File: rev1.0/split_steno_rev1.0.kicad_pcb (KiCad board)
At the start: 2 copper layers, 97.6 x 84.5 mm, 50 parts, among them J0 Audio-Jack-4, K0 KEYSW, K1 KEYSW, K10 KEYSW, K11 KEYSW, K12 KEYSW, K13 KEYSW, K14 KEYSW, K15 KEYSW, K16 KEYSW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

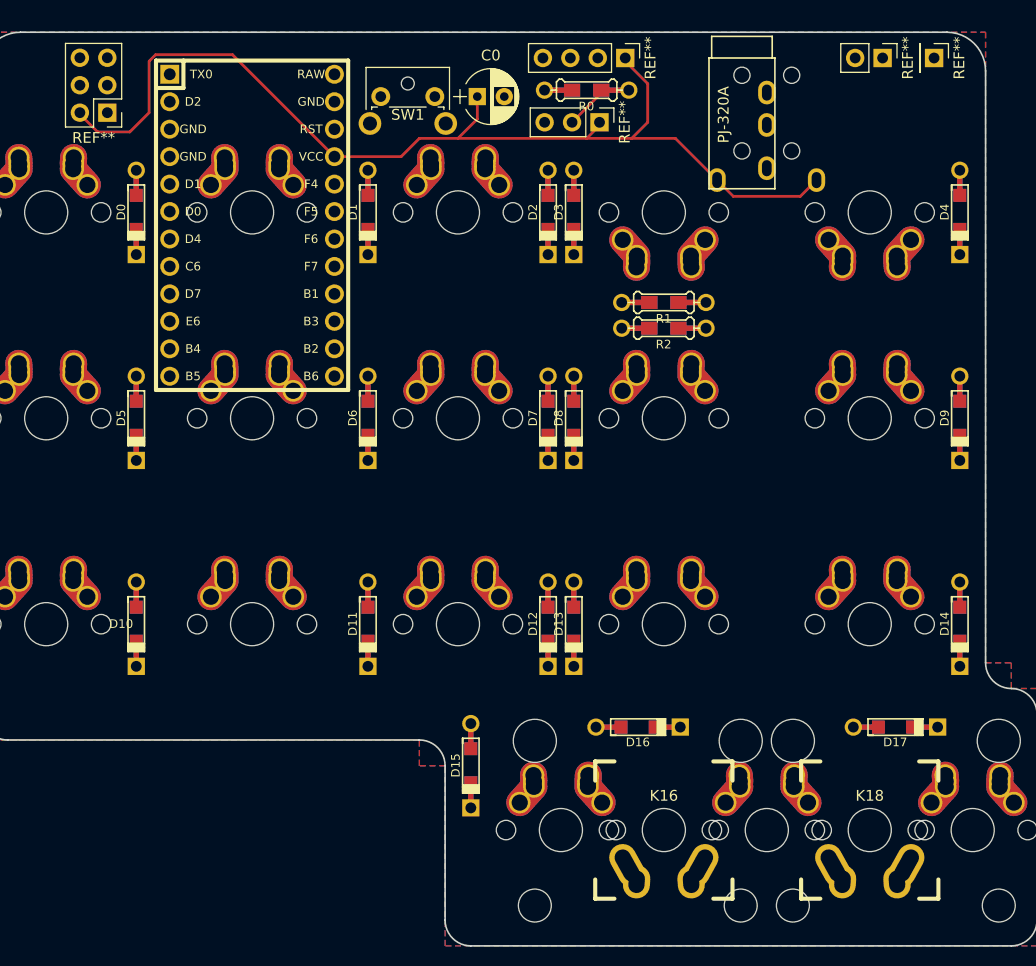
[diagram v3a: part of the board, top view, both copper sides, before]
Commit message: updated schematic and footprints
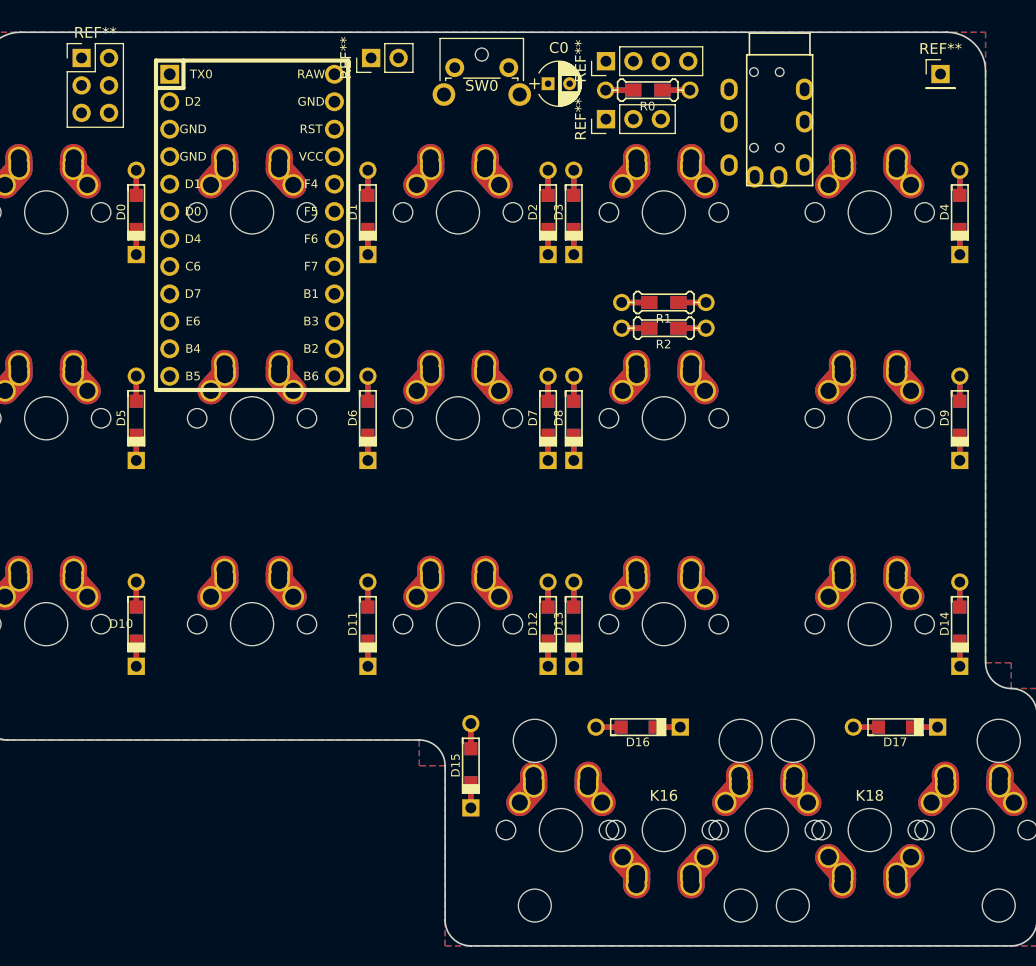
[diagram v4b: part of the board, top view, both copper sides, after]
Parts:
- removed SW1: SW_PUSH, Keebio-Parts:SW_Tactile_SPST_Angled_MJTP1117
- added G***: LOGO, airi_logo:airi_icon-7.6, F.Cu at (126.2, 96.1)
- added G***: LOGO, airi_logo:airi_icon-7.6, B.Cu at (126.2, 96.1)
- added REF**: TRRS-PJ-320A, Keebio-Parts:TRRS-PJ-320A, B.Cu at (172.6, 73.5)
- added SW0: SW_PUSH, Keebio-Parts:SW_Tactile_SPST_Angled_MJTP1117, F.Cu at (145.0, 74.7)
- C0: footprint Capacitors_THT:CP_Radial_D5.0mm_P2.50mm -> Capacitors_THT:CP_Radial_D4.0mm_P2.00mm
- J0: footprint Keebio-Parts:TRRS-PJ-320A-dual -> Keebio-Parts:TRRS-PJ-320A
- K16, K18: footprint Keebio-Parts:Hybrid_PCB_200H-dual -> Keebio-Parts:Hybrid_PCB_200H-dual-nosilk
- REF**: value EXTRA -> PWM
- moved REF** 47.3 mm to (137.2, 73.8), turned to 90 degrees
- moved C0 6.66 mm to (153.6, 76.2)
- moved R0 5.66 mm to (162.8, 76.8)
- moved REF** 5.59 mm to (110.4, 73.8), turned to 0 degrees
- moved REF** 1.81 mm to (158.9, 74.1), turned to 90 degrees
- moved REF** 1.60 mm to (189.9, 75.3), turned to 0 degrees
- moved J0 1.23 mm to (175.0, 73.5)
- moved REF** 0.67 mm to (158.9, 79.5), turned to 90 degrees
- turned K3 to 0 degrees
- turned K4 to 0 degrees
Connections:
- net /col1 renamed /c1
- net Net-(U0-Pad1) renamed /tx
- net Net-(U0-Pad14) renamed /miso
- net Net-(U0-Pad15) renamed /sclk
- net Net-(U0-Pad16) renamed /mosi
- D0 pad 1: /row0 -> /r0
- D1 pad 1: /row0 -> /r0
- D10 pad 1: /row2 -> /r2
- D11 pad 1: /row2 -> /r2
- D12 pad 1: /row2 -> /r2
- D13 pad 1: /row2 -> /r2
- D14 pad 1: /row2 -> /r2
- D15 pad 1: /row3 -> /r3
- D16 pad 1: /row3 -> /r3
- D17 pad 1: /row3 -> /r3
- D2 pad 1: /row0 -> /r0
- D3 pad 1: /row0 -> /r0
- D4 pad 1: /row0 -> /r0
- D5 pad 1: /row1 -> /r1
- D6 pad 1: /row1 -> /r1
- D7 pad 1: /row1 -> /r1
- D8 pad 1: /row1 -> /r1
- D9 pad 1: /row1 -> /r1
- J0 pad 1: VCC -> /d0
- J0 pad 2: /data0 -> /d1
- J0 pad 3: /data1 -> VCC
- K0 pad 1: /col0 -> /c0
- K10 pad 1: /col0 -> /c0
- K12 pad 1: /col2 -> /c2
- K13 pad 1: /col3 -> /c3
- K14 pad 1: /col4 -> /c4
- K15 pad 1: /col2 -> /c2
- K16 pad 1: /col3 -> /c3
- K17 pad 1: /col3 -> /c3
- K18 pad 1: /col4 -> /c4
- K19 pad 1: /col4 -> /c4
- K2 pad 1: /col2 -> /c2
- K3 pad 1: /col3 -> /c3
- K4 pad 1: /col4 -> /c4
- K5 pad 1: /col0 -> /c0
- K7 pad 1: /col2 -> /c2
- K8 pad 1: /col3 -> /c3
- K9 pad 1: /col4 -> /c4
- R0 pad 2: /rgb0 -> /d2
- R1 pad 1: /data0 -> VCC
- R1 pad 2: VCC -> /d1
- R2 pad 1: /data1 -> VCC
- R2 pad 2: VCC -> /d0
- REF** pad 2: VCC -> (no net)
- REF** pad 6: GND -> (no net)
- REF** pad 1: VCC -> (no net) (x2)
- REF** pad 2: GND -> (no net) (x2)
- REF** pad 2: /dout -> (no net)
- REF** pad 3: GND -> (no net)
- U0 pad 10: /rgb0 -> /pwm
- U0 pad 18: /row3 -> /r0
- U0 pad 19: /row2 -> /c4
- U0 pad 2: /data0 -> /d0
- U0 pad 20: /row1 -> /c3
- U0 pad 21: VCC -> /c2
- U0 pad 23: GND -> (no net)
- U0 pad 3: GND -> /d1
- U0 pad 4: GND -> /d2
- U0 pad 5: Net-(U0-Pad5) -> /c0
- U0 pad 7: /col2 -> /r1
- U0 pad 8: /col3 -> /r2
- U0 pad 9: /col4 -> /r3
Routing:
- net VCC: track 97.7 -> 0.00 mm
- net /dout: track 6.48 -> 0.00 mm

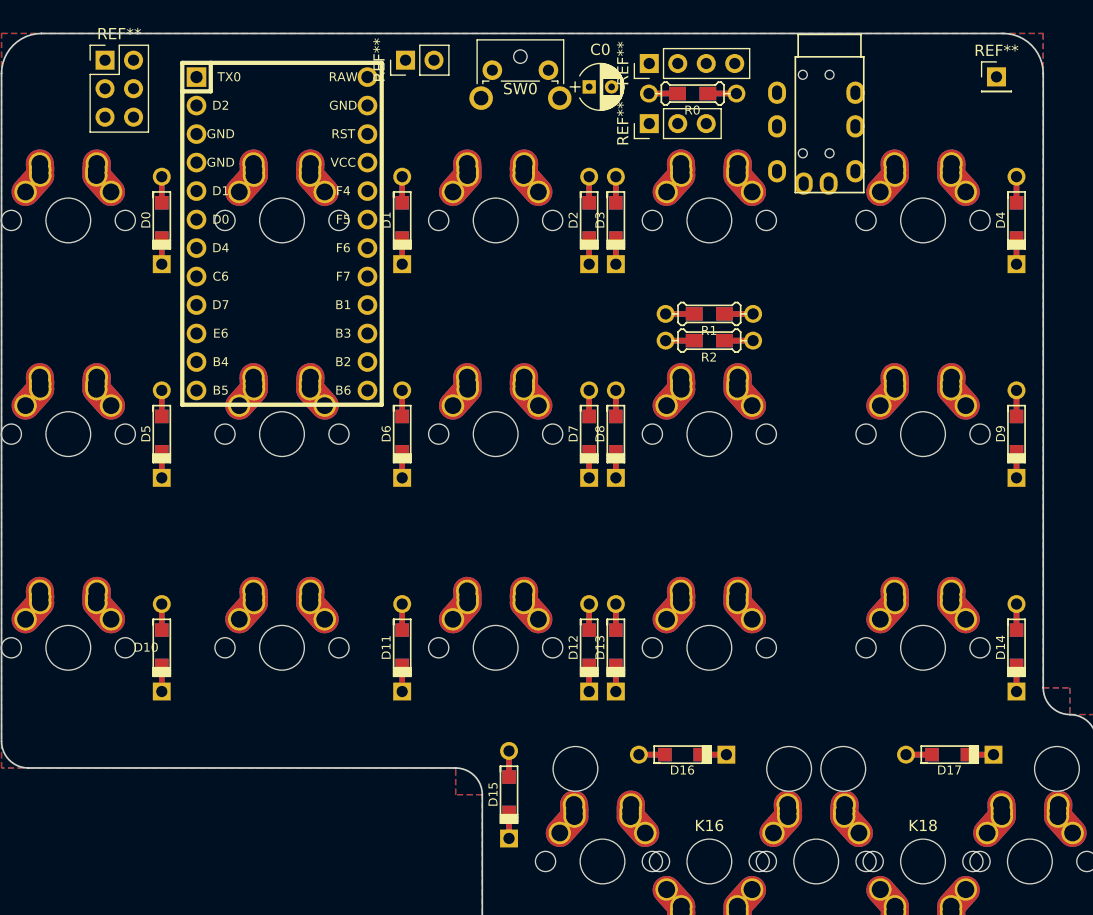
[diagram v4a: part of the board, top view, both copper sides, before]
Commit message: rearranged footprints
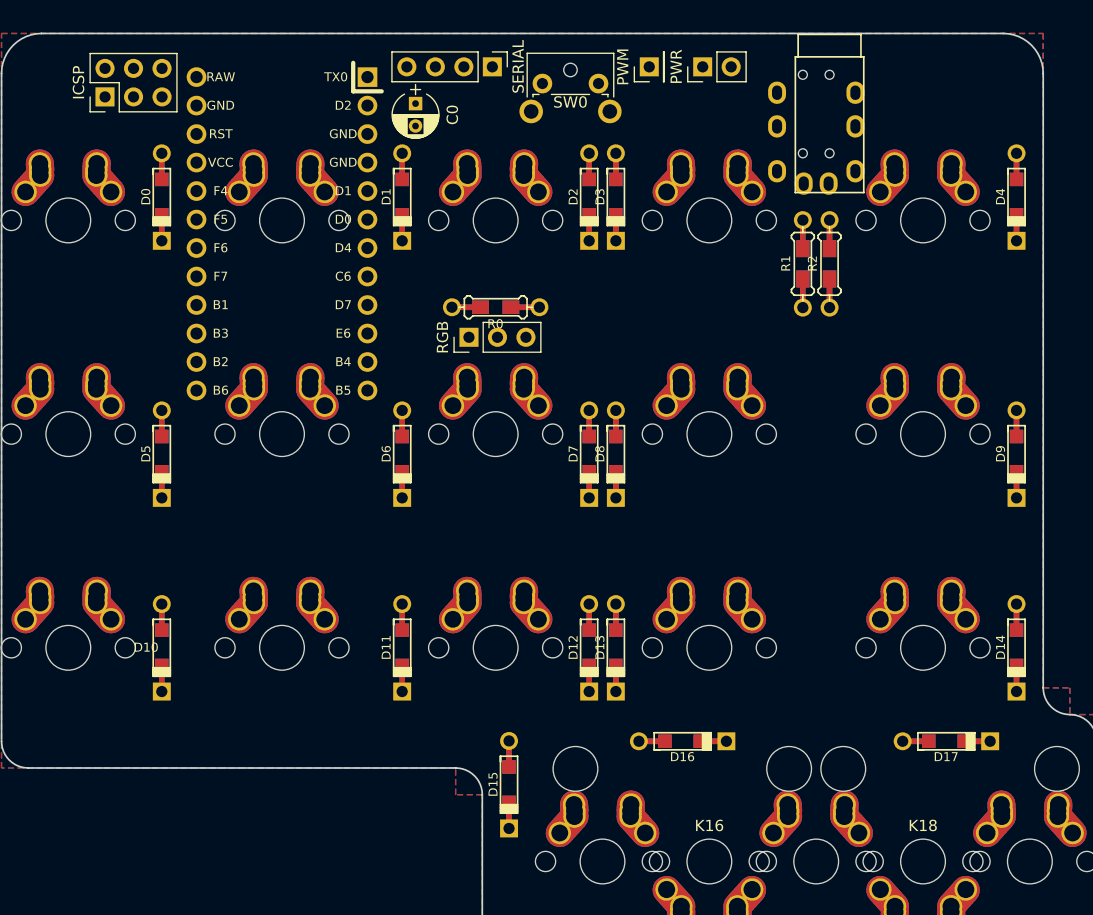
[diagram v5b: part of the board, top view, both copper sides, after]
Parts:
- removed G*** (x2): LOGO, airi_logo:airi_icon-7.6
- J0: value Audio-Jack-4 -> TRRS
- REF**: value TRRS-PJ-320A -> TRRS
- U0: moved to B.Cu
- moved PWM 31.0 mm to (158.9, 74.4), turned to 90 degrees
- moved PWR 26.5 mm to (163.7, 74.4)
- moved R0 25.9 mm to (145.3, 95.8)
- moved RGB 24.9 mm to (142.9, 98.5)
- moved C0 15.5 mm to (138.1, 77.7), turned to 270 degrees
- moved SERIAL 14.0 mm to (145.0, 74.4), turned to 270 degrees
- moved R2 12.7 mm to (175.0, 92.0), turned to 270 degrees
- moved R1 9.46 mm to (172.6, 92.0), turned to 270 degrees
- moved SW0 4.62 mm to (149.4, 75.9)
- moved ICSP 3.27 mm to (110.4, 77.1), turned to 90 degrees
- moved D4 2.08 mm to (191.7, 86.0)
- moved D3 2.08 mm to (156.0, 86.0)
- moved D2 2.08 mm to (153.6, 86.0)
- moved D1 2.08 mm to (136.9, 86.0)
- moved D0 2.08 mm to (115.5, 86.0)
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- renumbered REF** to ICSP, REF** to PWM, REF** to PWR, REF** to RGB, REF** to SERIAL
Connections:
- ICSP pad 1: (no net) -> /miso
- ICSP pad 2: (no net) -> VCC
- ICSP pad 3: (no net) -> /sclk
- ICSP pad 4: (no net) -> /mosi
- ICSP pad 6: (no net) -> GND
- PWR pad 2: (no net) -> GND
- REF** pad 1: (no net) -> /d0
- REF** pad 2: (no net) -> /d1
- RGB pad 1: (no net) -> VCC
- RGB pad 2: (no net) -> /dout
- RGB pad 3: (no net) -> GND
- SERIAL pad 1: (no net) -> VCC
- SERIAL pad 2: (no net) -> GND

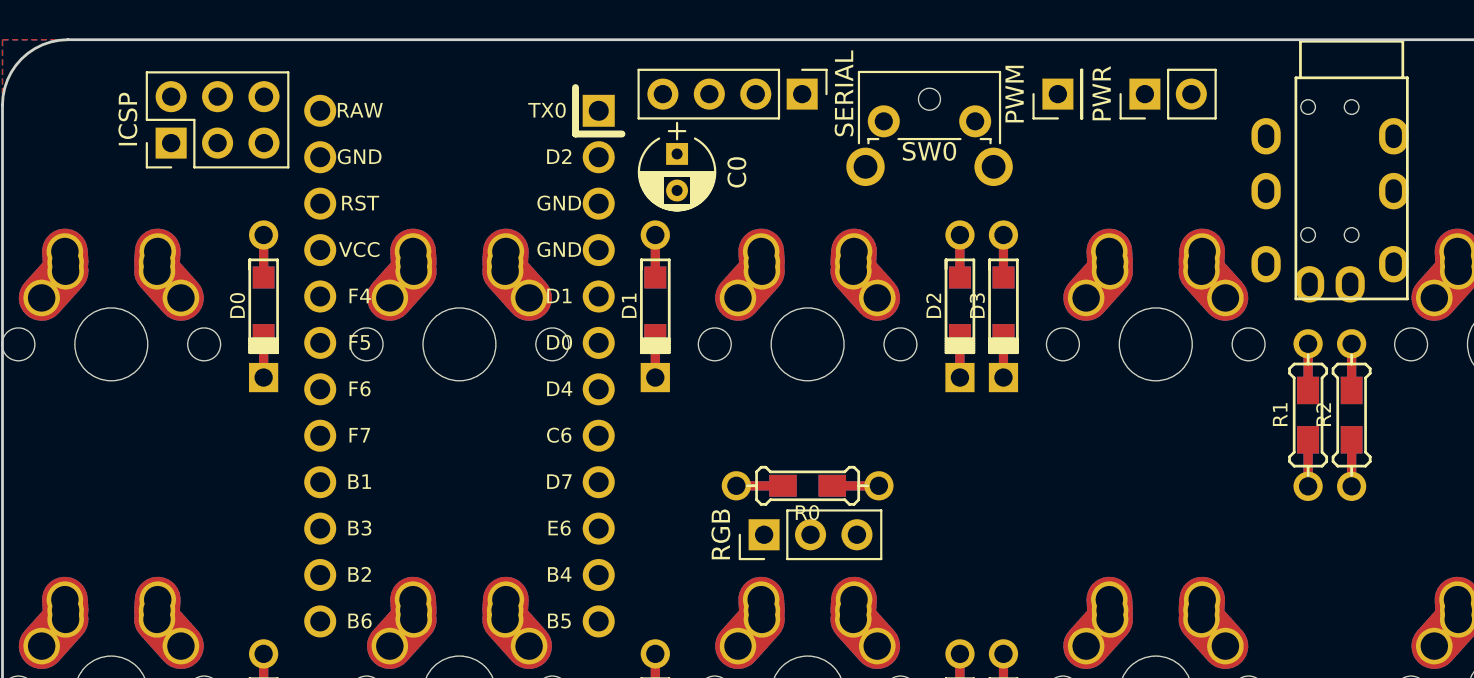
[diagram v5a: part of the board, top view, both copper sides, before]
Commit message: reorganized schematic library and pro micro footprint
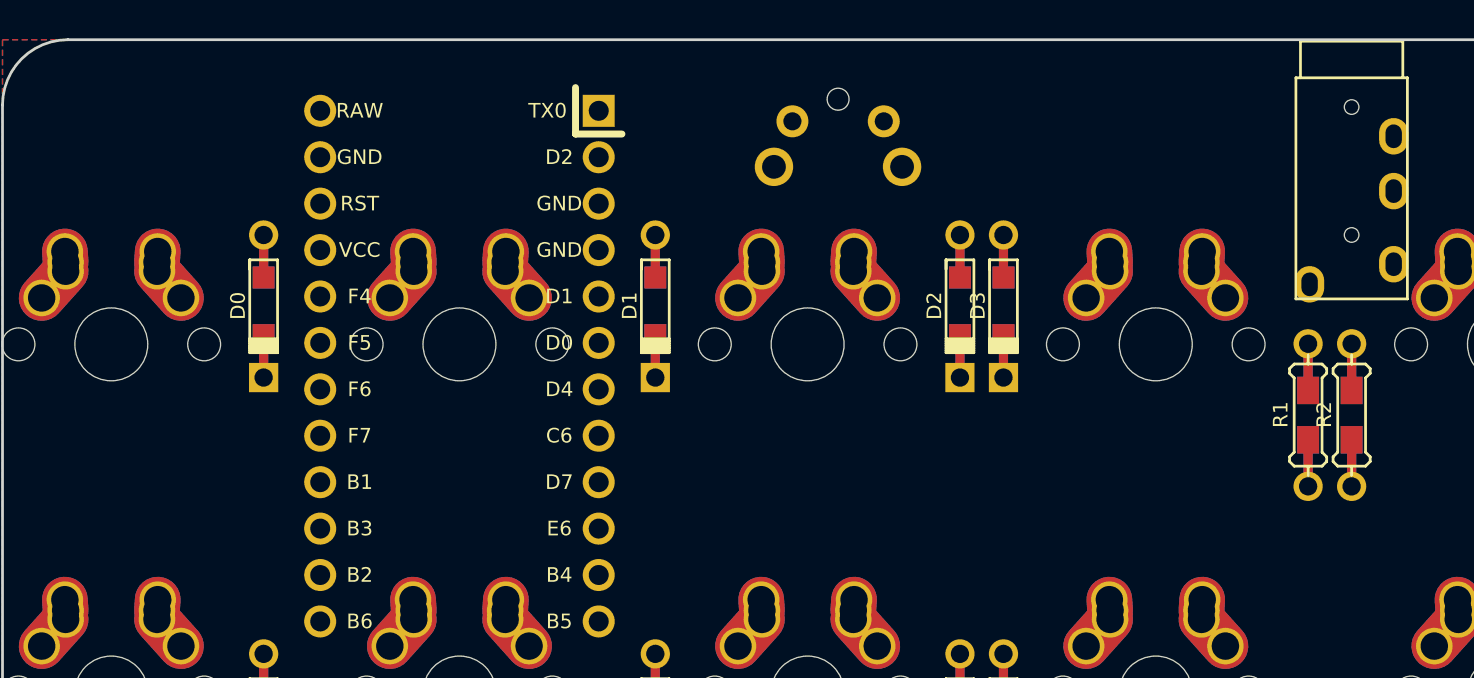
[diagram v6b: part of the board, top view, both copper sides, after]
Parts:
- removed C0: CP, Capacitors_THT:CP_Radial_D4.0mm_P2.00mm
- removed ICSP: ICSP, Pin_Headers:Pin_Header_Straight_2x03_Pitch2.54mm
- removed PWM: PWM, Pin_Headers:Pin_Header_Straight_1x01_Pitch2.54mm
- removed PWR: PWR, Pin_Headers:Pin_Header_Straight_1x02_Pitch2.54mm
- removed R0: 500, Keebio-Parts:Resistor-Hybrid
- removed REF**: TRRS, Keebio-Parts:TRRS-PJ-320A
- removed RGB: RGB, Pin_Headers:Pin_Header_Straight_1x03_Pitch2.54mm
- removed SERIAL: SERIAL, Pin_Headers:Pin_Header_Straight_1x04_Pitch2.54mm
- J0: value TRRS -> Audio-Jack-4
- SW0: moved to B.Cu
- turned SW0 to 180 degrees
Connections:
- U0 pad 10: /pwm -> /r1
- U0 pad 11: (no net) -> /r2
- U0 pad 12: (no net) -> /r3
- U0 pad 13: (no net) -> Net-(U0-Pad13)
- U0 pad 14: /miso -> Net-(U0-Pad14)
- U0 pad 15: /sclk -> Net-(U0-Pad15)
- U0 pad 16: /mosi -> Net-(U0-Pad16)
- U0 pad 17: (no net) -> /r0
- U0 pad 18: /r0 -> /c4
- U0 pad 19: /c4 -> /c3
- U0 pad 2: /d0 -> Net-(U0-Pad2)
- U0 pad 20: /c3 -> /c2
- U0 pad 21: /c2 -> VCC
- U0 pad 22: (no net) -> Net-(SW0-Pad1)
- U0 pad 23: (no net) -> GND
- U0 pad 24: (no net) -> Net-(U0-Pad24)
- U0 pad 3: /d1 -> GND
- U0 pad 4: /d2 -> GND
- U0 pad 5: /c0 -> /d0
- U0 pad 6: /c1 -> /d1
- U0 pad 7: /r1 -> Net-(U0-Pad7)
- U0 pad 8: /r2 -> /c0
- U0 pad 9: /r3 -> /c1

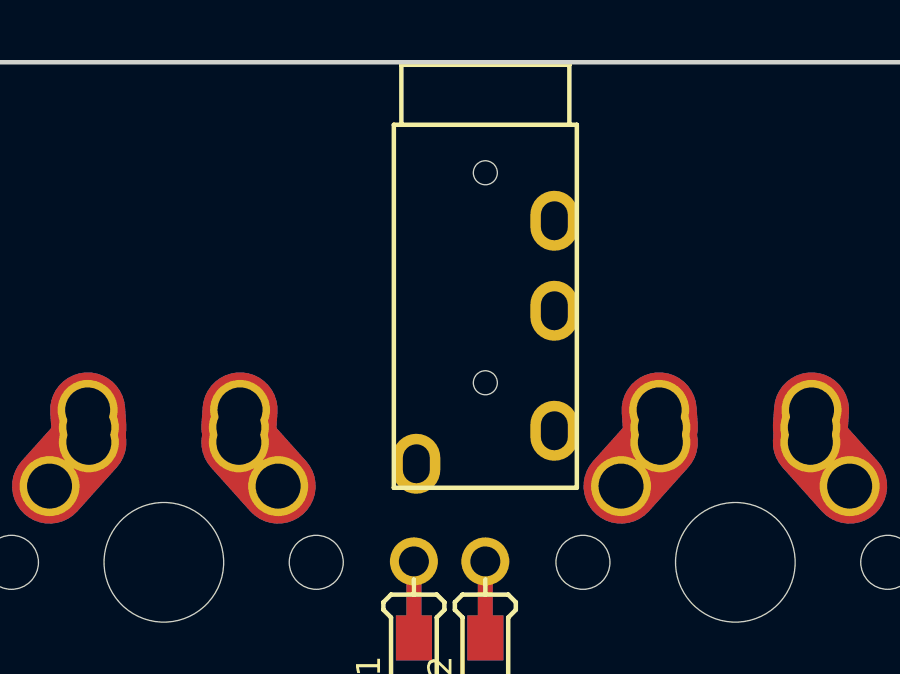
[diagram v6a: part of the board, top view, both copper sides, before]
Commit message: removed global libraries and moved to local versions
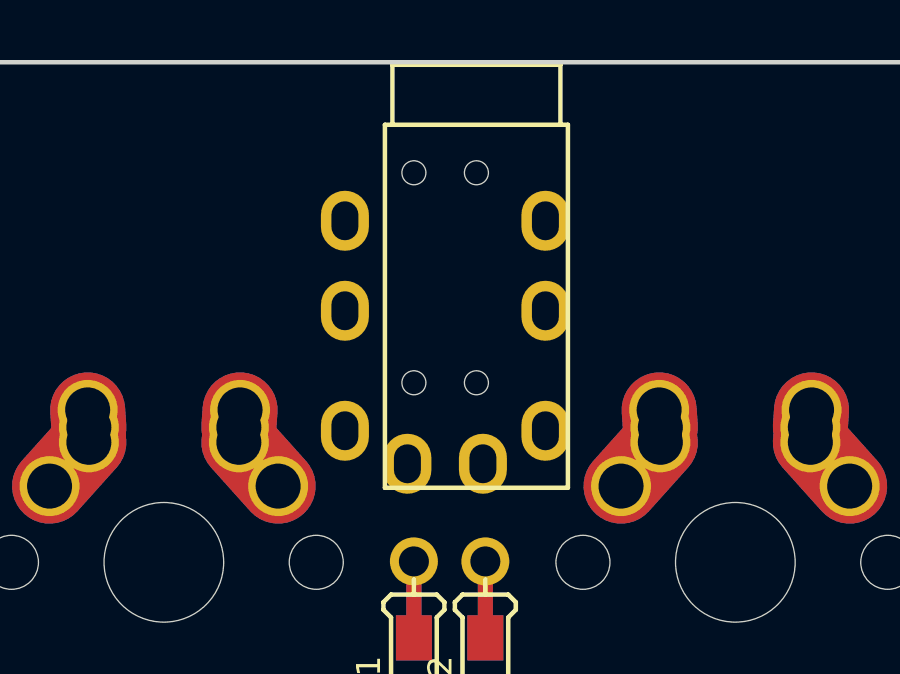
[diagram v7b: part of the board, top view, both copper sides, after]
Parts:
- added REF**: TRRS-PJ-320A, Keebio-Parts:TRRS-PJ-320A, B.Cu at (172.6, 73.5)
- J0: value Audio-Jack-4 -> TRRS
- moved J0 0.30 mm to (174.7, 73.5)
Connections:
- net /tx renamed Net-(U0-Pad1)
- J0 pad 3: VCC -> GND
- J0 pad 4: GND -> VCC
- K18 pad 2: Net-(K18-Pad2) -> Net-(D17-Pad2)
- R1 pad 1: VCC -> /d1
- R1 pad 2: /d1 -> VCC
- R2 pad 1: VCC -> /d0
- R2 pad 2: /d0 -> VCC
